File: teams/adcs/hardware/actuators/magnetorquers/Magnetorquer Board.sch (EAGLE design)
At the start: 29 parts

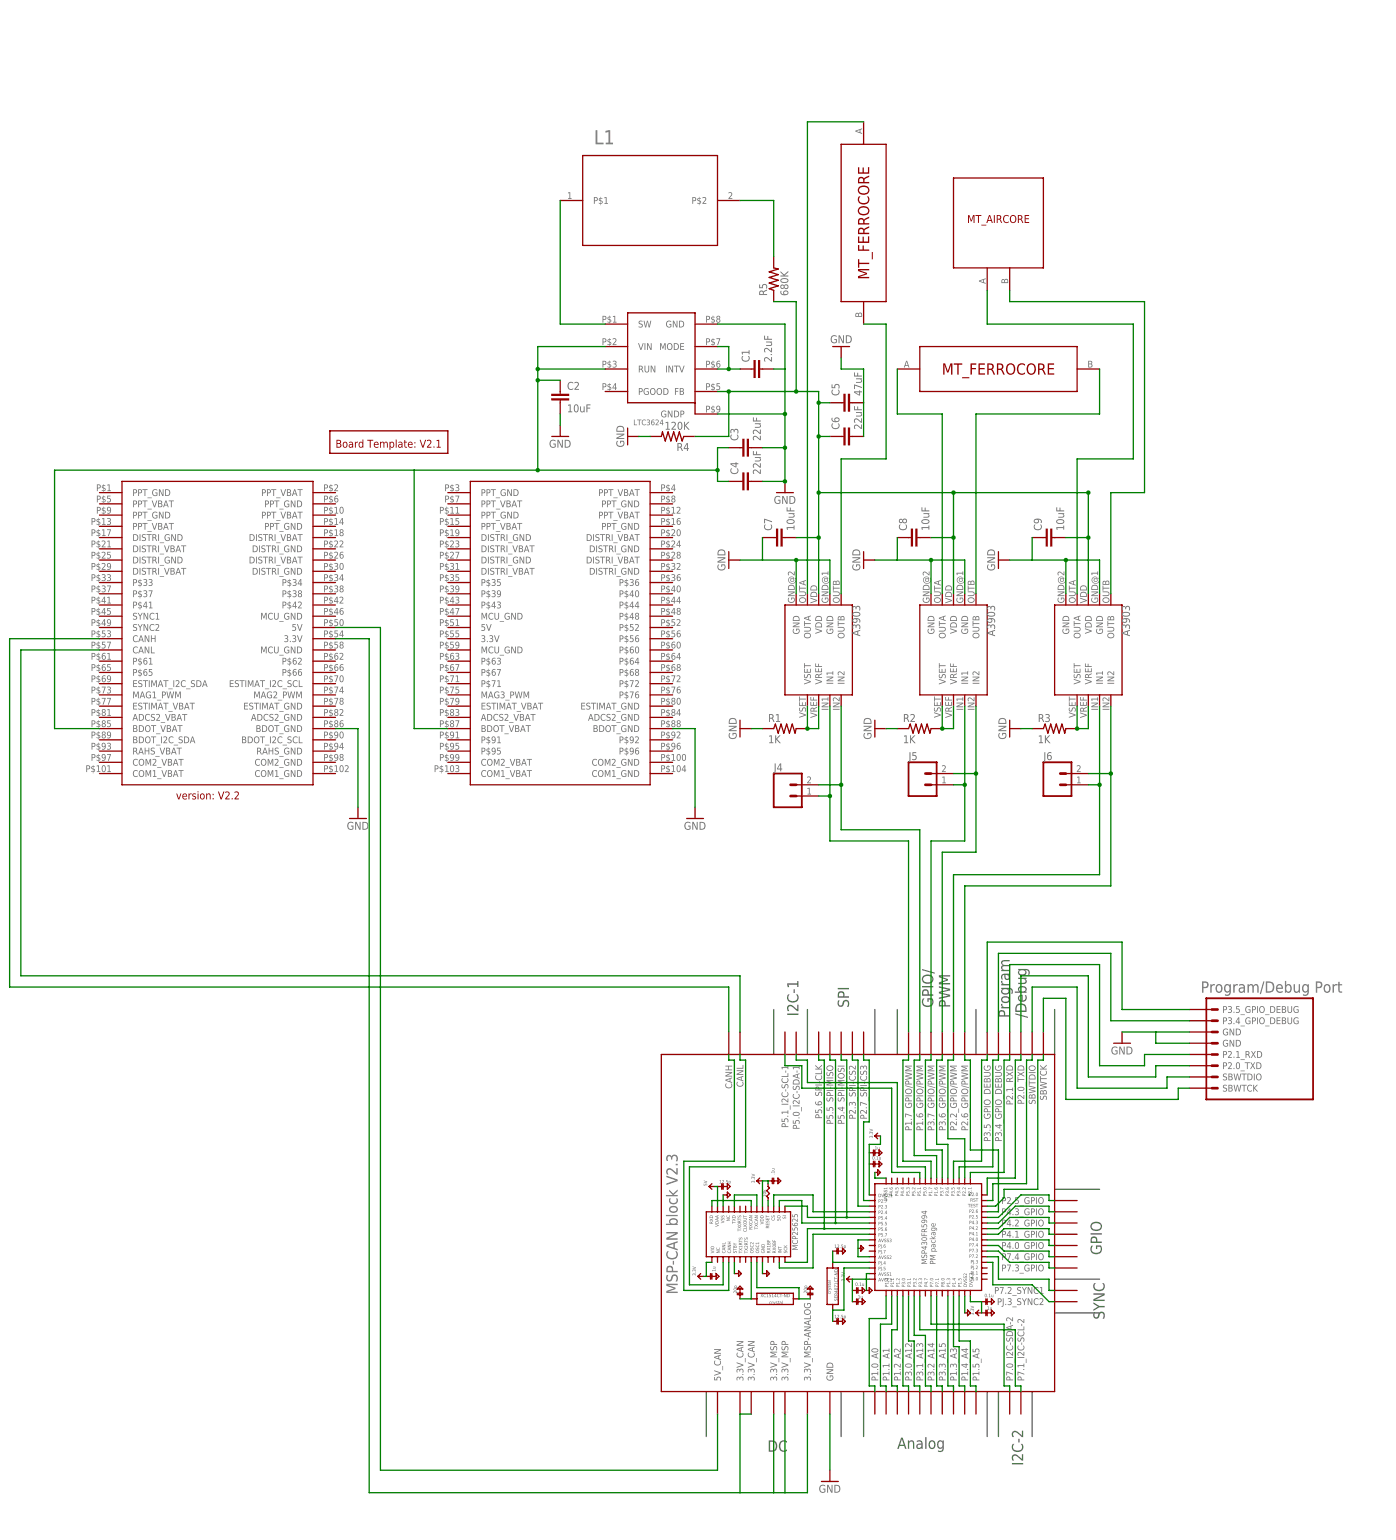
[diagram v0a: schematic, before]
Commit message: ADCS/MT: Switched from distributed 3V3/5V to LDOs
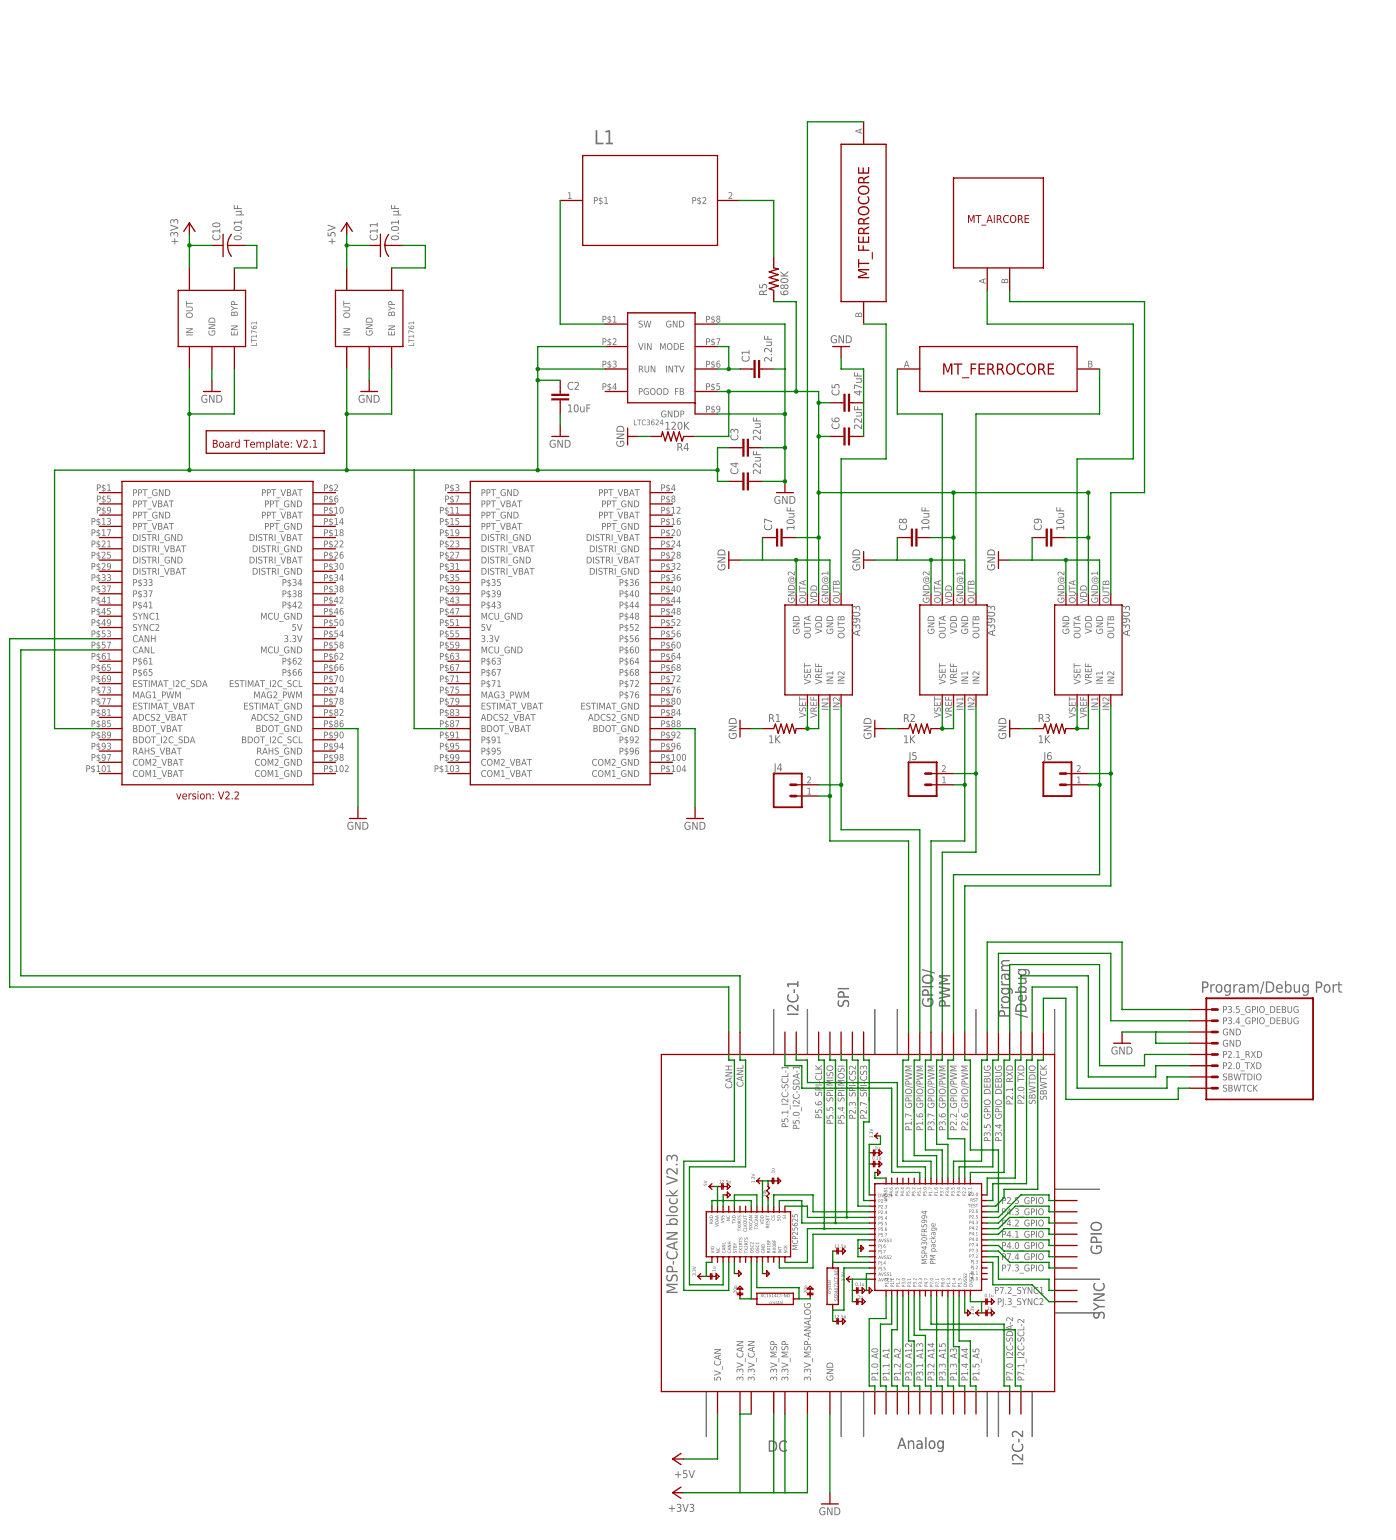
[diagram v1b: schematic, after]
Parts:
- added C10, C11: 0.01 μF, rcl:C-USC0805
- added LDO_3V3, LDO_5V: LINEAR_LDO_LT1761-X, DubSat1 Components:LINEAR_LDO_LT1761-X
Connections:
- removed net N$23: U$1.5V@50, U$7.5V_CAN
- removed net N$24: U$1.3.3V@54, U$7.3.3V_CAN@1, U$7.3.3V_CAN@2, U$7.3.3V_MSP-ANALOG@1, U$7.3.3V_MSP@2, U$7.3.3V_MSP@3
- new net +3V3: C10.1, LDO_3V3.OUT, U$7.3.3V_CAN@1, U$7.3.3V_CAN@2, U$7.3.3V_MSP-ANALOG@1, U$7.3.3V_MSP@2, U$7.3.3V_MSP@3
- new net +5V: C11.1, LDO_5V.OUT, U$7.5V_CAN
- new net N$26: C10.2, LDO_3V3.BYP
- new net N$33: C11.2, LDO_5V.BYP
- net GND: now also LDO_3V3.GND, LDO_5V.GND
- net N$19: now also LDO_3V3.EN, LDO_3V3.IN, LDO_5V.EN, LDO_5V.IN

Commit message: ADCS/MT: Routed LDOs and cleaned up schematic
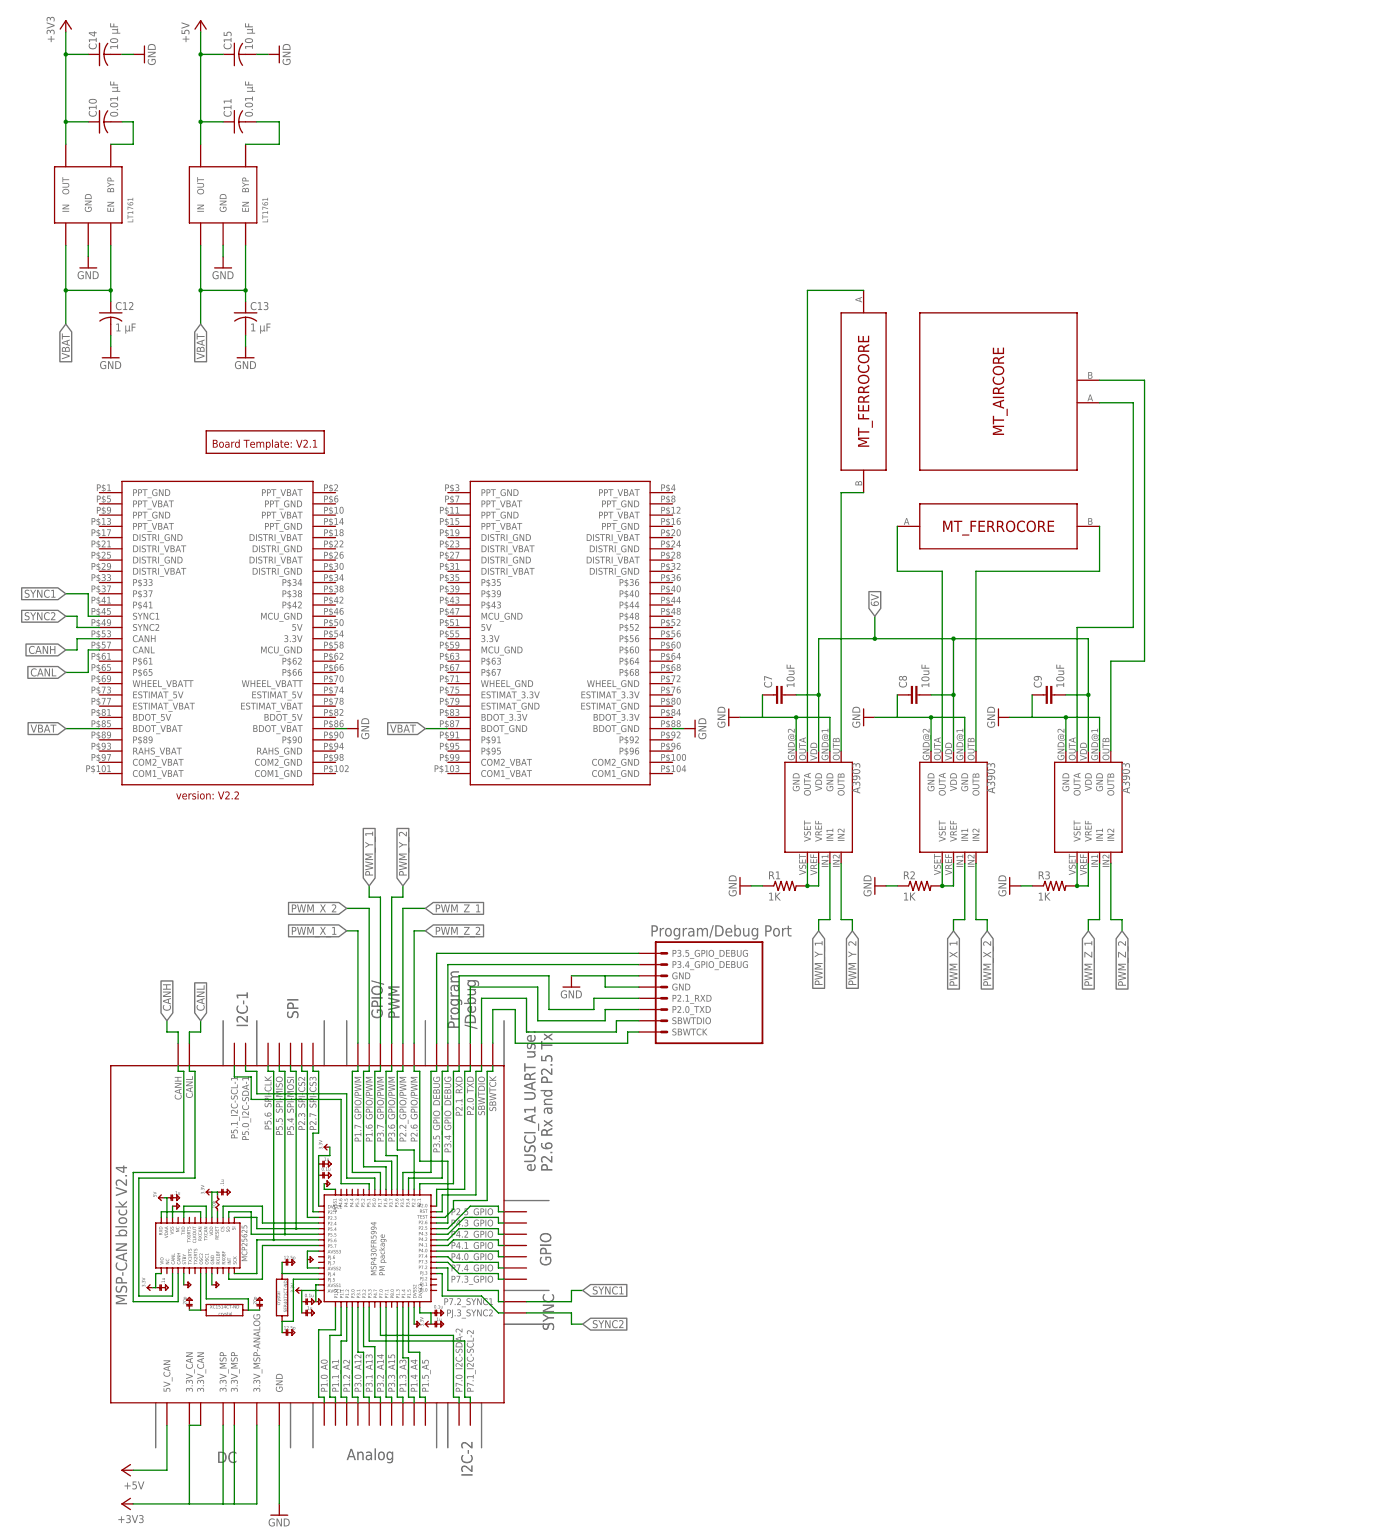
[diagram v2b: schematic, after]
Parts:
- removed C1: 2.2uF, rcl:C-EUC0805
- removed C2: 10uF, SparkFun-Capacitors:CAP0805
- removed C3, C4, C6: 22uF, rcl:C-EUC1206
- removed C5: 47uF, rcl:C-EUC1206
- removed J4, J5, J6: (no value), SparkFun-Connectors:CONN_02
- removed L1: (no value), inductors:XAL4030-332ME
- removed R4: 120K, rcl:R-US_R0805
- removed R5: 680K, rcl:R-US_R0805
- removed U$6: LINEAR_BUCK_LTC3624, ICs:LINEAR_BUCK_LTC3624
- added C12, C13: 1 μF, rcl:C-USC0805
- added C14, C15: 10 μF, rcl:C-USC0805
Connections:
- net N$21 renamed CANH
- net N$22 renamed CANL
- removed net N$16: C5.1, C6.1, C7.2, C8.2, C9.2, R4.1, R5.1, U$6.FB, U1.VDD, U2.VDD, U3.VDD
- removed net N$17: C1.1, U$6.INTV, U$6.MODE
- removed net N$19: C2.1, C3.1, C4.1, LDO_3V3.EN, LDO_3V3.IN, LDO_5V.EN, LDO_5V.IN, U$1.BDOT_VBAT@85, U$1.BDOT_VBAT@87, U$6.RUN, U$6.VIN
- removed net N$20: L1.P$1, U$6.SW
- removed net N$25: L1.P$2, R5.2
- removed net N$3: J4.1, U$7.P1.7_GPIO/PWM, U1.IN1
- removed net N$4: J5.1, U$7.P3.7_GPIO/PWM, U2.IN1
- removed net N$5: J6.1, U$7.P2.2_GPIO/PWM, U3.IN1
- removed net N$6: J6.2, U$7.P2.6_GPIO/PWM, U3.IN2
- removed net N$8: J5.2, U$7.P3.6_GPIO/PWM, U2.IN2
- removed net N$9: J4.2, U$7.P1.6_GPIO/PWM, U1.IN2
- new net 6V: C7.2, C8.2, C9.2, U1.VDD, U2.VDD, U3.VDD
- new net PWM_X_1: U$7.P1.7_GPIO/PWM, U2.IN1
- new net PWM_X_2: U$7.P1.6_GPIO/PWM, U2.IN2
- new net PWM_Y_1: U$7.P3.7_GPIO/PWM, U1.IN1
- new net PWM_Y_2: U$7.P3.6_GPIO/PWM, U1.IN2
- new net PWM_Z_1: U$7.P2.2_GPIO/PWM, U3.IN1
- new net PWM_Z_2: U$7.P2.6_GPIO/PWM, U3.IN2
- new net SYNC1: U$1.SYNC1, U$7.P7.2_SYNC1
- new net SYNC2: U$1.SYNC2, U$7.PJ.3_SYNC2
- new net VBAT: C12.1, C13.1, LDO_3V3.EN, LDO_3V3.IN, LDO_5V.EN, LDO_5V.IN, U$1.BDOT_GND@87, U$1.BDOT_VBAT@85
- net +3V3: now also C14.1
- net +5V: now also C15.1
- net GND: now also C12.2, C13.2, C14.2, C15.2, U$1.BDOT_VBAT@86; no longer C1.2, C2.2, C3.2, C4.2, C5.2, C6.2, R4.2, U$1.BDOT_GND@86, U$6.GND, U$6.GNDP
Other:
- moved on the sheet: C10, C11, C7, C8, C9, R1, R2, R3
